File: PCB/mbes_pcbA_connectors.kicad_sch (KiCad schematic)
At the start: 35 parts, among them K1 HK19F-DCxxV-SHC, Q2 BC817, Q3 TPCA8120,L1Q, Q4 BC817, U2 L7805

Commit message: Small fixes
- Floating BC817's base fixed
- EngReady_LED connector orientation fixed
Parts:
- added R13: 100K, Resistor_SMD:R_1206_3216Metric, symbol Device:R
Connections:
- net GND: now also R13.1
- net at D1.1 (K), Q2.1 (B), R8.2: now also R13.2
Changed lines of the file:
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@@
 	)
 	(junction
+		(at 162.1028 67.564)
+		(diameter 0)
+		(color 0 0 0 0)
+	)
+	(junction
 		(at 65.532 114.046)
 		(diameter 0)
@@
 	)
 	(junction
+		(at 173.99 85.852)
+		(diameter 0)
+		(color 0 0 0 0)
+	)
+	(junction
 		(at 203.708 47.752)
 		(diameter 0)
@@
 	(wire
 		(pts
+			(xy 162.1028 67.564) (xy 173.99 67.564)
+		)
+		(stroke
+			(width 0)
+			(type default)
+		)
+	)
+	(wire
+		(pts
 			(xy 167.894 62.484) (xy 162.1028 62.484)
 		)
@@
 	(wire
 		(pts
-			(xy 162.052 85.852) (xy 203.708 85.852)
+			(xy 162.052 85.852) (xy 173.99 85.852)
 		)
 		(stroke
@@
 	(wire
 		(pts
+			(xy 173.99 85.852) (xy 203.708 85.852)
+		)
+		(stroke
+			(width 0)
+			(type default)
+		)
+	)
+	(wire
+		(pts
 			(xy 195.834 35.052) (xy 195.834 42.672)
 		)
@@
 	(wire
 		(pts
+			(xy 173.99 75.184) (xy 173.99 67.564)
+		)
+		(stroke
+			(width 0)
+			(type default)
+		)
+	)
+	(wire
+		(pts
 			(xy 77.216 66.167) (xy 94.996 66.167)
 		)
@@
 	(wire
 		(pts
+			(xy 173.99 82.804) (xy 173.99 85.852)
+		)
+		(stroke
+			(width 0)
+			(type default)
+		)
+	)
+	(wire
+		(pts
 			(xy 179.832 115.824) (xy 176.022 115.824)
 		)
@@
 					(unit 1)
 				)
+			)
+		)
+	)
+	(symbol
+		(lib_id "Device:R")
+		(at 173.99 78.994 180)
+		(unit 1)
+		(exclude_from_sim no)
+		(in_bom yes)
+		(on_board yes)
+		(dnp no)
+		(property "Reference" "R13"
+			(at 167.6908 78.994 90)
+			(effects
+				(font
+					(size 1.27 1.27)
+				)
+				(hide yes)
+			)
+		)
+		(property "Value" "100K"
+			(at 174.0408 79.0448 90)
+			(effects
+				(font
+					(size 1.27 1.27)
+				)
+			)
+		)
+		(property "Footprint" "Resistor_SMD:R_1206_3216Metric"
+			(at 175.768 78.994 90)
+			(effects
+				(font
+					(size 1.27 1.27)
+				)
+				(hide yes)
+			)
+		)
+		(property "Datasheet" "~"
+			(at 173.99 78.994 0)
+			(effects
+				(font
+					(size 1.27 1.27)
+				)
+				(hide yes)
+			)
+		)
+		(property "Description" ""
+			(at 173.99 78.994 0)
+			(effects
+				(font
+					(size 1.27 1.27)
+				)
+				(hide yes)
+			)
+		)
+		(pin "1"
+		)
+		(pin "2"
+		)
+		(instances
+			(project "main"
+				(path "/709d0967-afe5-49d3-92a5-d2bb94550bdb/3216a3d3-5416-4017-b51b-dad2d5be039c"
+					(reference "R13")
+					(unit 1)
+				)

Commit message: Connectors changing
In order to reuse the already used cables, all the input signal connectors have been changed from solder-wires-sockets to pin-header connectors.
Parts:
- Decomp_1, LightOnOff_sw1, addLights1, clutch_sw1, extpwr1, powerOFF1: footprint Connector_Wire:SolderWire-0.75sqmm_1x02_P4.8mm_D1.25mm_OD2.3mm -> Connector_PinHeader_2.54mm:PinHeader_1x02_P2.54mm_Vertical
- GND-1, GND-2: footprint Connector_Wire:SolderWire-1.5sqmm_1x03_P6mm_D1.7mm_OD3mm -> Connector_Wire:SolderWire-1sqmm_1x03_P5.4mm_D1.4mm_OD2.7mm
- leftCtrls_conn1, rightCtrls_conn1: footprint Custom_conn_wire:SolderWire-0.25sqmm_1x06_P4.2mm_D1.0mm_OD2.2mm -> Connector_PinHeader_2.54mm:PinHeader_1x06_P2.54mm_Vertical
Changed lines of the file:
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@@
 			)
 		)
-		(property "Footprint" "Connector_Wire:SolderWire-0.75sqmm_1x02_P4.8mm_D1.25mm_OD2.3mm"
+		(property "Footprint" "Connector_PinHeader_2.54mm:PinHeader_1x02_P2.54mm_Vertical"
 			(at 56.642 130.302 0)
 			(effects
@@
 			)
 		)
-		(property "Footprint" "Custom_conn_wire:SolderWire-0.25sqmm_1x06_P4.2mm_D1.0mm_OD2.2mm"
+		(property "Footprint" "Connector_PinHeader_2.54mm:PinHeader_1x06_P2.54mm_Vertical"
 			(at 56.388 96.774 0)
 			(effects
@@
 			)
 		)
-		(property "Footprint" "Connector_Wire:SolderWire-0.75sqmm_1x02_P4.8mm_D1.25mm_OD2.3mm"
+		(property "Footprint" "Connector_PinHeader_2.54mm:PinHeader_1x02_P2.54mm_Vertical"
 			(at 56.388 114.046 0)
 			(effects
@@
 			)
 		)
-		(property "Footprint" "Connector_Wire:SolderWire-1.5sqmm_1x03_P6mm_D1.7mm_OD3mm"
+		(property "Footprint" "Connector_Wire:SolderWire-1sqmm_1x03_P5.4mm_D1.4mm_OD2.7mm"
 			(at 137.668 88.392 0)
 			(effects
@@
 			)
 		)
-		(property "Footprint" "Connector_Wire:SolderWire-0.75sqmm_1x02_P4.8mm_D1.25mm_OD2.3mm"
+		(property "Footprint" "Connector_PinHeader_2.54mm:PinHeader_1x02_P2.54mm_Vertical"
 			(at 56.642 135.89 0)
 			(effects
@@
 			)
 		)
-		(property "Footprint" "Connector_Wire:SolderWire-1.5sqmm_1x03_P6mm_D1.7mm_OD3mm"
+		(property "Footprint" "Connector_Wire:SolderWire-1sqmm_1x03_P5.4mm_D1.4mm_OD2.7mm"
 			(at 137.668 98.806 0)
 			(effects
@@
 			)
 		)
-		(property "Footprint" "Connector_Wire:SolderWire-0.75sqmm_1x02_P4.8mm_D1.25mm_OD2.3mm"
+		(property "Footprint" "Connector_PinHeader_2.54mm:PinHeader_1x02_P2.54mm_Vertical"
 			(at 56.388 180.594 0)
 			(effects
@@
 			)
 		)
-		(property "Footprint" "Connector_Wire:SolderWire-0.75sqmm_1x02_P4.8mm_D1.25mm_OD2.3mm"
+		(property "Footprint" "Connector_PinHeader_2.54mm:PinHeader_1x02_P2.54mm_Vertical"
 			(at 56.642 168.91 0)
 			(effects
@@
 			)
 		)
-		(property "Footprint" "Custom_conn_wire:SolderWire-0.25sqmm_1x06_P4.2mm_D1.0mm_OD2.2mm"
+		(property "Footprint" "Connector_PinHeader_2.54mm:PinHeader_1x06_P2.54mm_Vertical"
 			(at 56.388 71.882 0)
 			(effects
@@
 			)
 		)
-		(property "Footprint" "Connector_Wire:SolderWire-0.75sqmm_1x02_P4.8mm_D1.25mm_OD2.3mm"
+		(property "Footprint" "Connector_PinHeader_2.54mm:PinHeader_1x02_P2.54mm_Vertical"
 			(at 56.3372 162.4076 0)
 			(effects

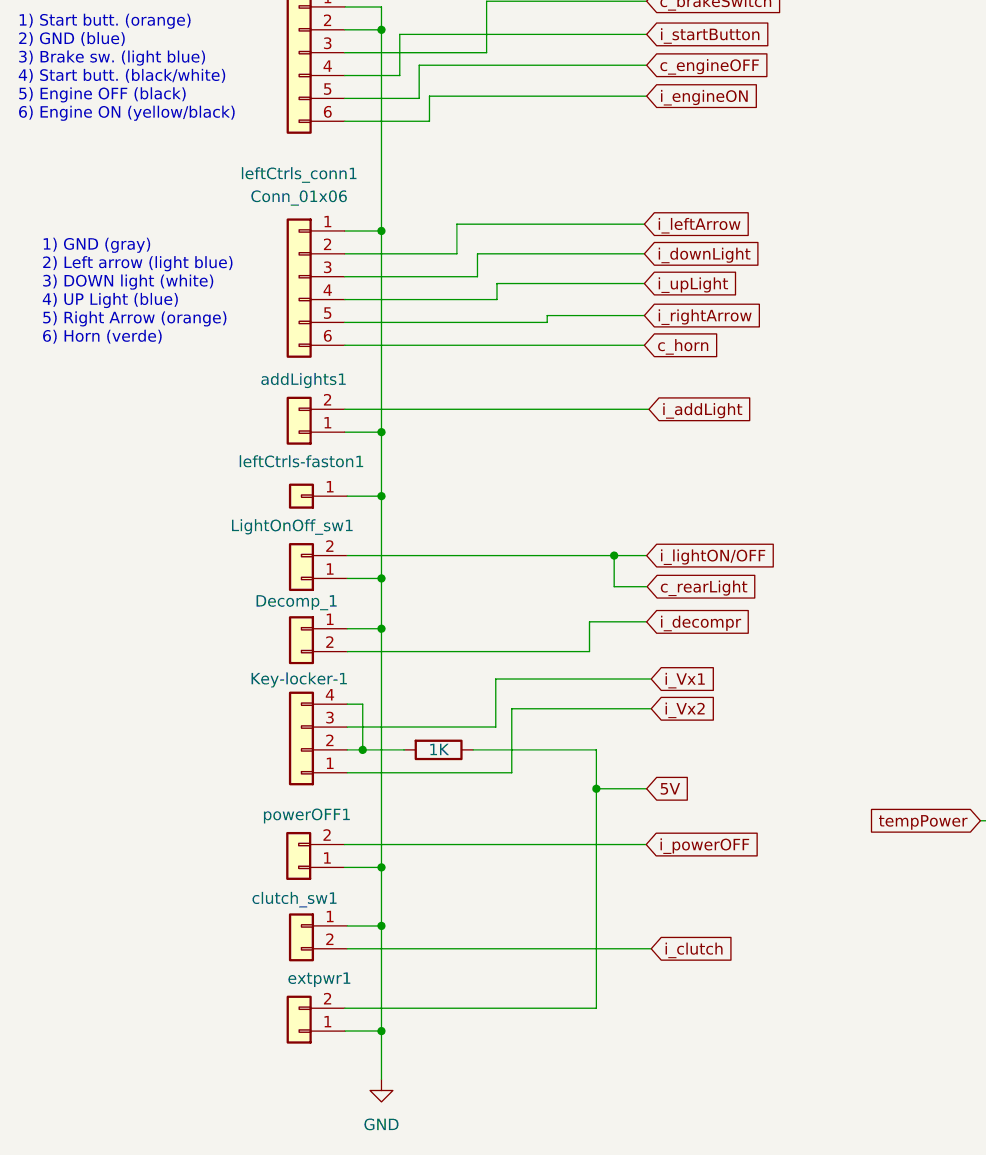
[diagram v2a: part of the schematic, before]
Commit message: onnectors number reducing
Because clucth lever switch is always placed in the left side of the handle-bar, I added the pin to the left-controls connector.
The 6-pins connector has been substituted by an 8-pins one.
In this way I got two advantages:
- I have reduced the command cables in the upside of the PCB
- The left and right controls connectors are different, now
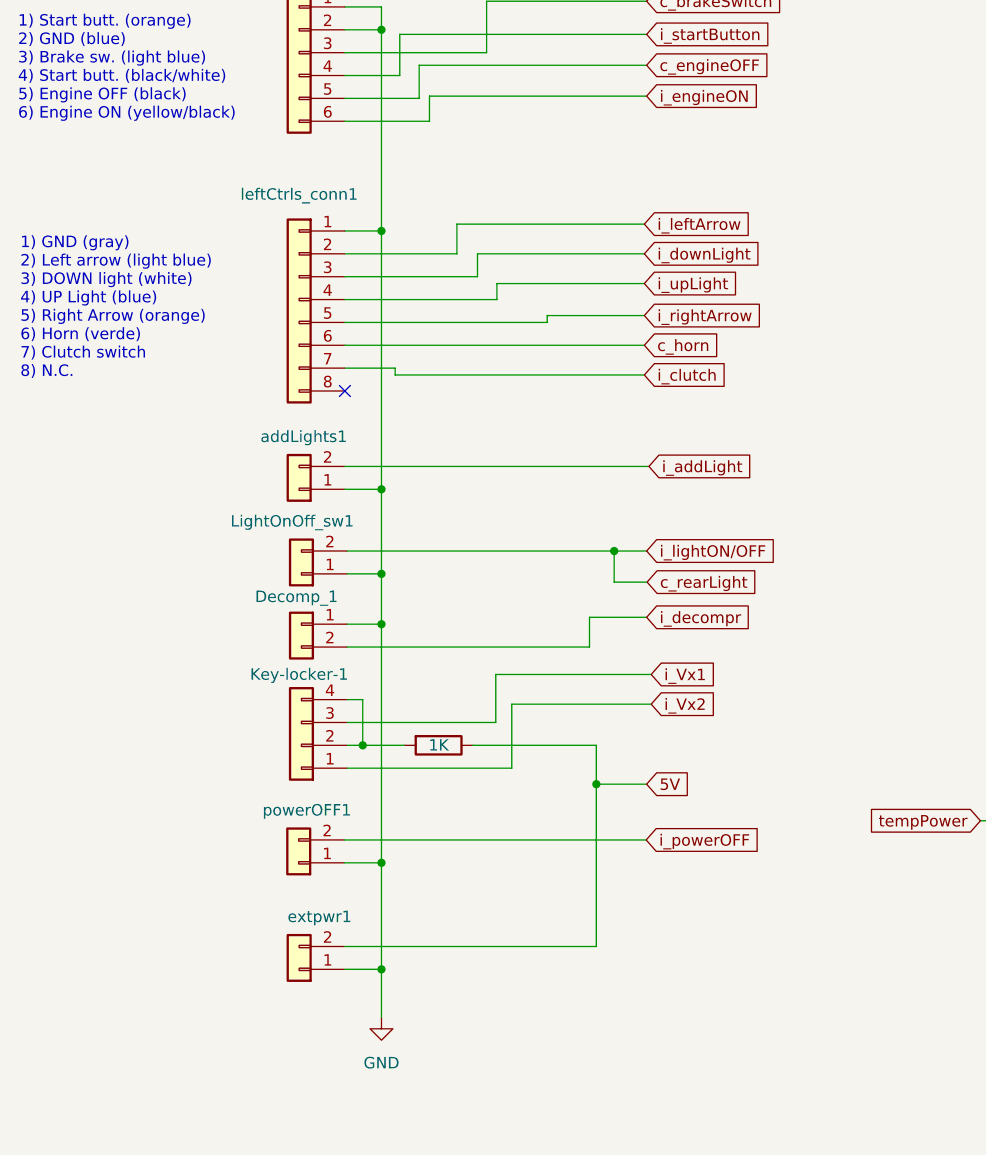
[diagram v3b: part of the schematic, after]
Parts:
- removed clutch_sw1: Conn_01x02, Connector_PinHeader_2.54mm:PinHeader_1x02_P2.54mm_Vertical, symbol Connector_Generic:Conn_01x02
- removed leftCtrls-faston1: Conn_01x01, Connector_Wire:SolderWire-0.5sqmm_1x01_D0.9mm_OD2.1mm, symbol Connector_Generic:Conn_01x01
- removed leftCtrls_conn1: Conn_01x06, Connector_PinHeader_2.54mm:PinHeader_1x06_P2.54mm_Vertical, symbol Connector_Generic:Conn_01x06
- added leftCtrls_conn1: Conn_01x08, Connector_PinHeader_2.54mm:PinHeader_1x08_P2.54mm_Vertical, symbol Connector_Generic:Conn_01x08
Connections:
- net GND: now also leftCtrls_conn1.1 (Pin_1)
- net c_horn: now also leftCtrls_conn1.6 (Pin_6)
- net i_clutch: now also leftCtrls_conn1.7 (Pin_7)
- net i_downLight: now also leftCtrls_conn1.3 (Pin_3)
- net i_leftArrow: now also leftCtrls_conn1.2 (Pin_2)
- net i_rightArrow: now also leftCtrls_conn1.5 (Pin_5)
- net i_upLight: now also leftCtrls_conn1.4 (Pin_4)
- no-connect marks 2 -> 3
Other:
- note added: "1) GND (gray) 2) Left arrow (light blue) 3) DOWN light (white) 4) UP Light (blue) 5) Right Arrow (orange) 6) Horn (verde) 7) Clutch switch 8) N.C."
- note removed: "1) GND (gray) 2) Left arrow (light blue) 3) DOWN light (white) 4) UP Light (blue) 5) Right Arrow (orange) 6) Horn (verde)"
- moved on the sheet: Decomp_1, Key-locker-1, LightOnOff_sw1, addLights1, extpwr1, powerOFF1

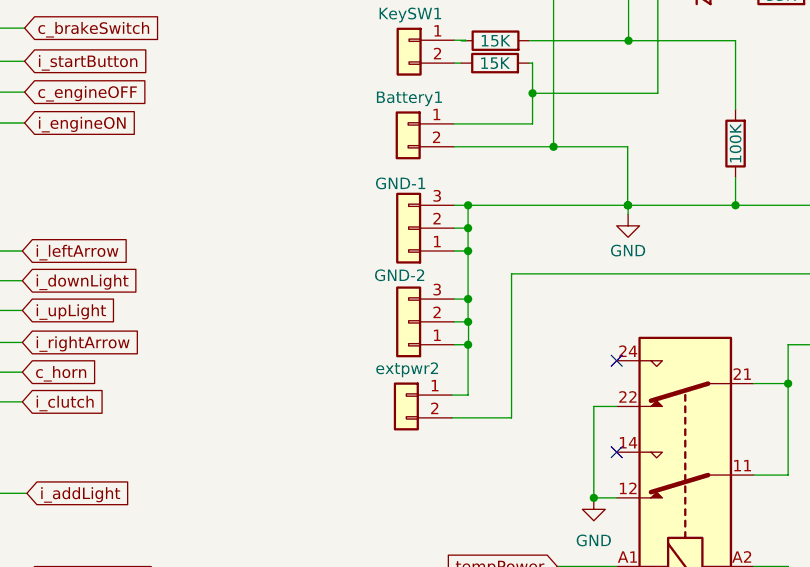
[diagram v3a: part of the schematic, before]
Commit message: Less unordered cables
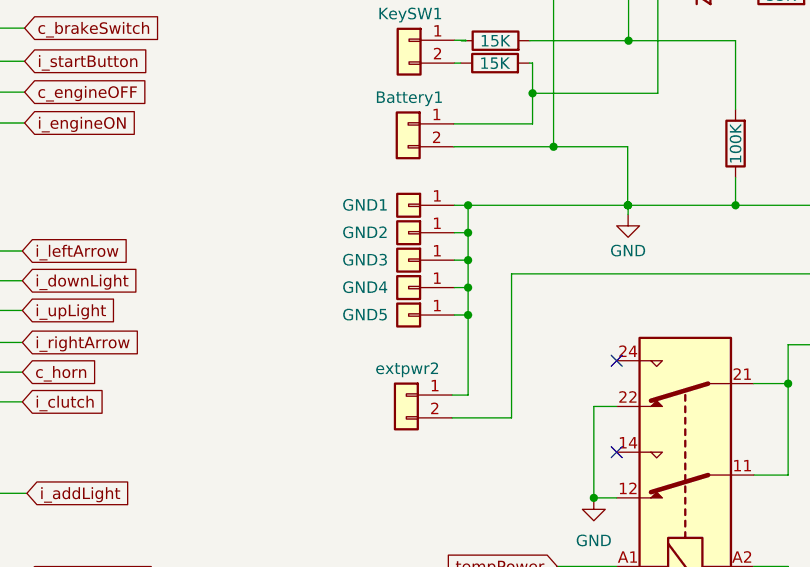
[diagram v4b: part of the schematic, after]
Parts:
- removed GND-1, GND-2: ~, Connector_Wire:SolderWire-1sqmm_1x03_P5.4mm_D1.4mm_OD2.7mm, symbol Connector_Generic:Conn_01x03
- added GND1, GND2, GND3, GND4, GND5: Conn_01x01, Connector_Wire:SolderWire-1sqmm_1x01_D1.4mm_OD2.7mm, symbol Connector_Generic:Conn_01x01
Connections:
- net GND: now also GND1.1 (Pin_1), GND2.1 (Pin_1), GND3.1 (Pin_1), GND4.1 (Pin_1), GND5.1 (Pin_1)
